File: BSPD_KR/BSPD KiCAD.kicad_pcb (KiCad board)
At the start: 2 copper layers, 52.2 x 80.9 mm, 71 parts, among them J1 Conn_01x03, J2 Conn_01x02, J3 Conn_01x02, K1 G5Q-1A4-DC12, Q1 2N7002, Q3 2N7002, U18 SN74AHCT1G08DBVR, U19 LM339N, U4 LM7805MPX/NOPB, U5 LM339N, U6 SN74AHC1G02DBVR, U9 SN74LVC1G04DBVT

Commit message: feat(bspd): lay out SR latch on PCB, fix board outline and via drill
Place U20/U21 (SN74AHC1G02 latch) on the bottom side under R30/D10,
R30/D10/C13 on the freed R19/R21/C11 sites and C14 decoupling below.
Route the new nets with Freerouting; existing nets unchanged within
1.5 mm. Drop C15 (one shared decoupling cap is enough for two adjacent
gates) and switch D10 to the DO-41 footprint already used by D9.

Also close the Edge.Cuts outline (small endpoint mismatches made the
Specctra exporter reject the board) and raise via drill to 0.3 mm to
meet the board's own min-hole constraint. DRC: 0 errors, 0 unconnected.

Co-Authored-By: Claude Fable 5.1 <noreply@anthropic.com>
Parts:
- removed C11: 10uF, Capacitor_THT:CP_Radial_D5.0mm_P2.50mm
- removed Q3: 2N7002, Package_TO_SOT_SMD:SOT-23
- removed R19: 1k, Resistor_THT:R_Axial_DIN0207_L6.3mm_D2.5mm_P10.16mm_Horizontal
- removed R21: 1M, Resistor_THT:R_Axial_DIN0207_L6.3mm_D2.5mm_P10.16mm_Horizontal
- added C13: 0.22uF, Kicad_Libraries:FA14X7R1H224KNU00, F.Cu at (-176.6, 108.7)
- added C14: 0.1uF, Kicad_Libraries:FA18X7R1H104KNU00, F.Cu at (-168.5, 109.8)
- added D10: 1N4148, Diode_THT:D_DO-41_SOD81_P10.16mm_Horizontal, F.Cu at (-171.0, 106.7)
- added R30: 470k, Resistor_THT:R_Axial_DIN0207_L6.3mm_D2.5mm_P10.16mm_Horizontal, F.Cu at (-160.9, 103.3)
- added U20: SN74AHC1G02DBVR, Package_TO_SOT_SMD:SOT-23-5, B.Cu at (-165.5, 103.3)
- added U21: SN74AHC1G02DBVR, Package_TO_SOT_SMD:SOT-23-5, B.Cu at (-165.5, 107.0)
- R20: value 56k -> 39k
- renumbered REF** to H1, REF** to H2, REF** to H3, REF** to H4
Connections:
- U5 pad 8: /10s -> /LATCH_Q
- U9 pad 4: Net-(Q3-G) -> /BSPD_TRIP
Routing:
- net /POR: track 0.00 -> 18.9 mm
- net /10s: track 17.3 -> 0.00 mm
- net /LATCH_Q: track 0.00 -> 14.8 mm
- net /BSPD_TRIP: track 0.00 -> 13.7 mm, vias 0 -> 1
- net /LATCH_QN: track 0.00 -> 8.36 mm
- net +5V: track 231.5 -> 238.1 mm
- net Net-(Q3-G): track 5.63 -> 0.00 mm
- net Net-(Q3-S): track 2.62 -> 0.00 mm
- net GLV-: track 0.00 -> 2.00 mm, vias 0 -> 2
- net Net-(R26-Pad1): track 45.2 -> 46.5 mm
- net Net-(R13-Pad1): track 35.3 -> 36.6 mm
- net Net-(U5A--): track 21.1 -> 22.0 mm
- net Net-(R15-Pad1): track 44.3 -> 45.0 mm
- net GLV+: track 76.7 -> 77.3 mm

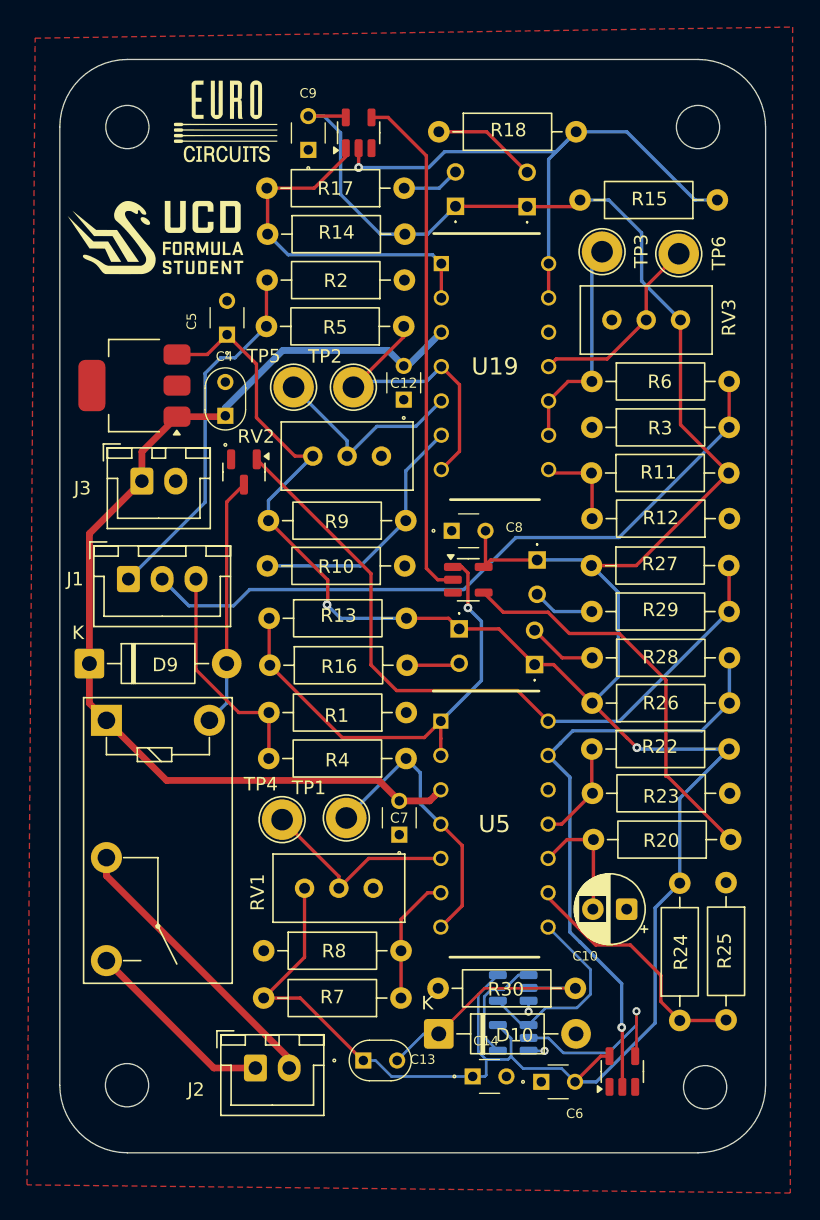
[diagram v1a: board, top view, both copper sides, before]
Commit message: fix(bspd): correct C10 electrolytic polarity, harden POR, enforce 0.25mm tracks
Full-chain behavioural sim (analysis/helpers/bspd_system.cir) showed the
POR pulse (220n/470k) could fall short of the AHC input threshold on a
slow 5V ramp, leaving the latch powered up in the tripped state. C13 is
now 10uF/100k (tau 1s), passing the worst-case ramp with margin.

The same pass found C10 (500ms timer cap) fitted with its positive pad on
GND while the timer node swings 0-5V; swapped the symbol orientation and
pad nets so the cap is forward biased. C13 uses the same part and
footprint. J2 nudged 0.5mm to clear the larger cap.

Re-routed the new nets with Freerouting at the board's 0.25mm minimum
track width (netclass default was 0.2, below the constraint). DRC: 0
errors, 0 unconnected; all pad nets match the schematic netlist.

Co-Authored-By: Claude Fable 5.1 <noreply@anthropic.com>
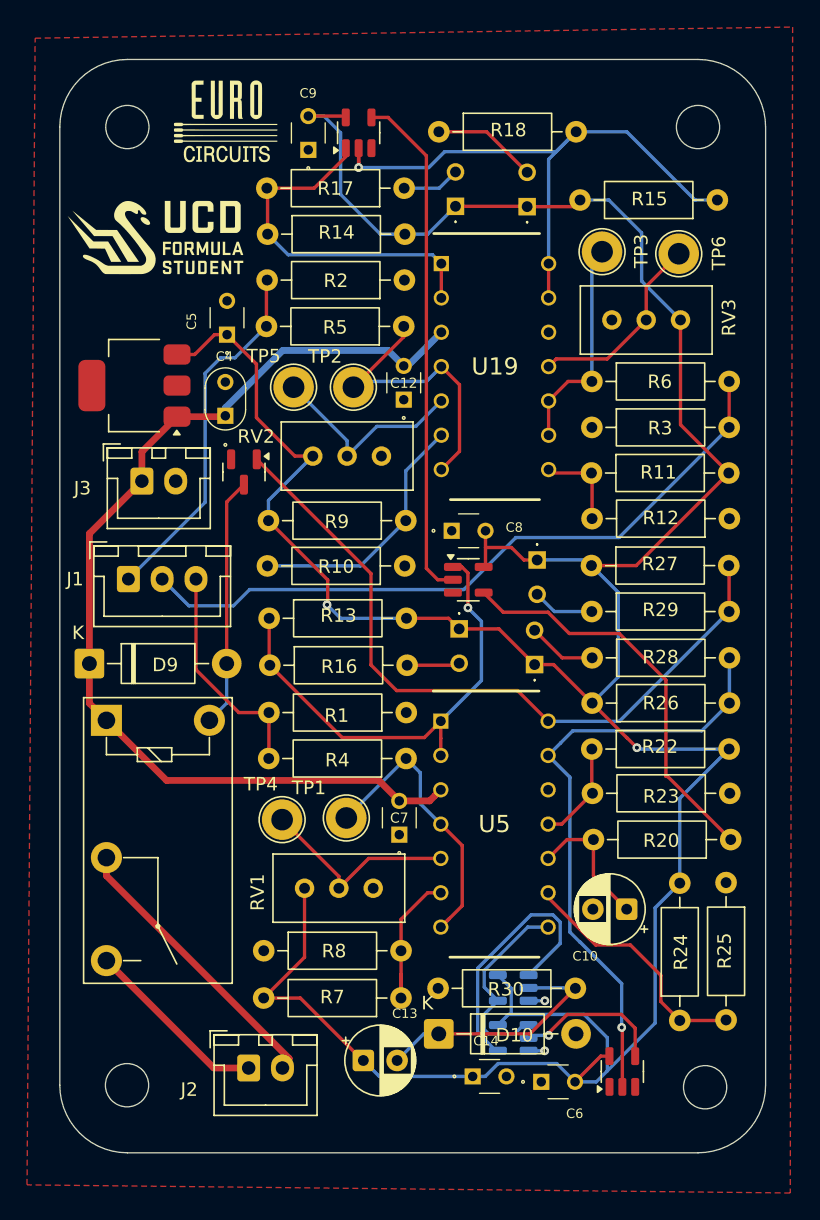
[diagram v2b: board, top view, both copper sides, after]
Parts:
- C13: value 0.22uF -> 10uF; footprint Kicad_Libraries:FA14X7R1H224KNU00 -> Capacitor_THT:CP_Radial_D5.0mm_P2.50mm
- moved J2 0.50 mm to (-185.1, 109.2)
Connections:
- C10 pad 1: GLV- -> /500ms
- C10 pad 2: /500ms -> GLV-
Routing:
- net /LATCH_QN: track 8.36 -> 19.7 mm
- net +5V: track 238.1 -> 242.0 mm
- net /BSPD_TRIP: track 13.7 -> 11.2 mm
- net Net-(U5B--): track 9.58 -> 11.3 mm
- net Net-(R26-Pad1): track 46.5 -> 45.2 mm
- net Net-(R13-Pad1): track 36.6 -> 35.3 mm
- net /500ms: track 9.10 -> 10.1 mm
- net BSPD_Shutdown+: track 14.3 -> 13.8 mm

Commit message: fix(bspd): sync PCB fields with schematic, refresh BOMs, add fab outputs
PCB footprint fields lagged the schematic after the latch/POR changes:
R30 still read 470k (schematic 100k), R20's part number was 56K (now
39K), D10 carried stale 1N4001 MPN/LCSC/datasheet fields, and Q1 had no
part number. Synced every field from the schematic via pcbnew; copper
and placement are untouched. DRC schematic parity now reports only the
H1-H4 mounting holes, which are PCB-only by design.

The root BOMs (BSPD BOM.csv, BSPD BOM_smd.csv) still listed the old RC
timer parts (Q3, R19, R21 1M, C11) and none of the latch ICs.
Regenerated them from the schematic in the same column format.

Adds fab/ (gerbers, drill, BOM, CPL) for the prototype order. The CPL
is regenerated for R30's value; the gerbers are unaffected because no
Fab layer is plotted. Also adds analysis/helpers/bspd_system.cir, the
full-chain sim cited in 69582c7.

Co-Authored-By: Claude Opus 5.5 <noreply@anthropic.com>
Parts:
- R30: value 470k -> 100k
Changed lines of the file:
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@@
 			)
 		)
-		(property "Part Number" "MCF 0.25W 56K"
+		(property "Part Number" "MCF 0.25W 39K"
 			(at 0 0 180)
 			(unlocked yes)
@@
 			)
 		)
-		(property "Datasheet" "http://www.vishay.com/docs/88503/1n4001.pdf"
+		(property "Datasheet" ""
 			(at 0 0 0)
 			(layer "F.Fab")
@@
 			)
 		)
-		(property "Description" ""
+		(property "Description" "Diode, small symbol"
 			(at 0 0 0)
 			(layer "F.Fab")
@@
 			)
 		)
-		(property "Manufacturer" "(MDD) Jiangsu Yutai Elec"
+		(property "Manufacturer" ""
 			(at 0 0 0)
 			(unlocked yes)
@@
 			)
 		)
-		(property "Manufacturer Part Number" "1N4001"
+		(property "Manufacturer Part Number" ""
 			(at 0 0 0)
 			(unlocked yes)
@@
 			)
 		)
-		(property "Store" "LCSC"
+		(property "Store" ""
 			(at 0 0 0)
 			(unlocked yes)
@@
 			)
 		)
-		(property "Store Part Number" "C2456"
+		(property "Store Part Number" ""
 			(at 0 0 0)
 			(unlocked yes)
@@
 			)
 		)
-		(property "Description" ""
+		(property "Description" "Unpolarized capacitor, small symbol"
 			(at 0 0 0)
 			(layer "F.Fab")
@@
 			)
 		)
+		(property "Part Number" "2N7002"
+			(at 0 0 0)
+			(layer "F.Fab")
+			(hide yes)
+			(effects
+				(font
+					(size 1.27 1.27)
+				)
+			)
+		)
 		(property ki_fp_filters "SOT?23*")
 		(sheetname "/")
@@
 			)
 		)
-		(property "Value" "470k"
+		(property "Value" "100k"
 			(at 5.08 2.37 0)
 			(layer "F.Fab")
@@
 			)
 		)
-		(property "Datasheet" "https://www.farnell.com/datasheets/3436052.pdf?_gl=1*6igt67*_gcl_au*OTY1ODIxNDc3LjE3MzU0MDg2OTk."
+		(property "Datasheet" ""
 			(at 0 0 0)
 			(layer "F.Fab")
@@
 			)
 		)
-		(property "Description" ""
+		(property "Description" "Resistor, small symbol"
 			(at 0 0 0)
 			(layer "F.Fab")
@@
 			)
 		)
-		(property "Part Number" "MCF 0.25W 470K"
+		(property "Part Number" "MCF 0.25W 100K"
 			(at 0 0 180)
 			(unlocked yes)
@@
 			)
 		)
-		(property "Description" ""
+		(property "Description" "Unpolarized capacitor, small symbol"
 			(at 0 0 0)
 			(layer "F.Fab")
@@
 			)
 		)
-		(property "Datasheet" "https://www.ti.com/lit/ds/symlink/sn74ahc1g02.pdf?ts=1738520903275"
+		(property "Datasheet" "https://www.ti.com/lit/ds/symlink/sn74ahc1g02.pdf"
 			(at 0 0 0)
 			(layer "B.Fab")
@@
 			)
 		)
-		(property "Datasheet" "https://www.ti.com/lit/ds/symlink/sn74ahc1g02.pdf?ts=1738520903275"
+		(property "Datasheet" "https://www.ti.com/lit/ds/symlink/sn74ahc1g02.pdf"
 			(at 0 0 0)
 			(layer "B.Fab")

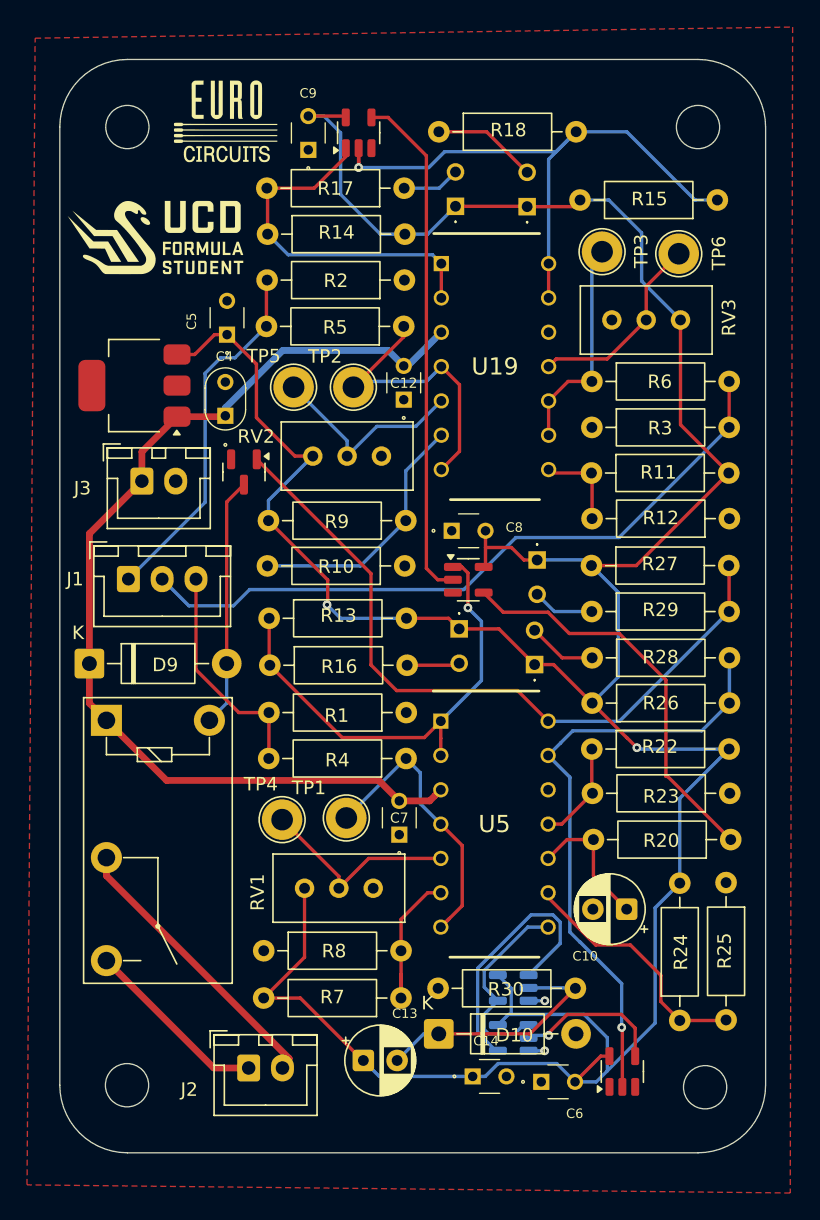
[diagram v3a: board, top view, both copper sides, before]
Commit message: feat(bspd): trip on any single sensor fault, lower missing threshold
An unplugged, open or shorted sensor did not trip the BSPD on its own:
the "sensor missing" comparators were wired-OR into the same wires as
"pressure/current too high", so a dead brake sensor looked like hard
braking and the board waited for high current (and vice versa).
T11.9.2 requires open circuit, short to ground and short to supply on
any SCS to reach the safe state (open SDC).

U5B, U19B and U19D now drive a separate FAULT_N net instead of the
per-sensor wires. Two LM393s (SOIC-8, bottom side, inside the U5/U19
footprints) add over-range checks at 4.74 V for all three sensors on
the same net. R32/C15 debounce FAULT_N (~0.16 s, glitches up to
~0.12 s ignored) and U22B pulls TRIP_REQ_N low, joining the existing
timer output, so a sensor fault latches exactly like an implausibility.

R8/R10/R12 go from 10k to 5.1k, moving the missing threshold from
0.45 V to 0.24 V: the TE M7139 brake sensors sit at 0.5 V at rest,
leaving only 0.05 V of margin before.

PCB: 10 new bottom-side parts. The three moved outputs were branch
points of their sensor wires, so those three spots were rerouted by
hand. New nets were routed with Freerouting with all existing tracks
locked; existing copper is otherwise unchanged. DRC 0 errors and 0
unconnected; parity shows only the H1-H4 mounting holes; the warning
set matches the previous board.

Sim: shared model in bspd_core.inc; bspd_fault_tests.cir covers each
sensor unplugged or shorted to 5 V (all trip in 0.16 s), 50/120 ms
glitches, full-scale and 30 bar braking alone, and late sensor
power-up (none trip). The original timeline results are unchanged.

Regenerated BOMs, fab outputs and the STEP model, which had dated
from before the latch rework. README updated, including the open item
that the current sensor must stay below 4.74 V (~224 A at 10 mV/A).

Co-Authored-By: Claude Opus 5.5 <noreply@anthropic.com>
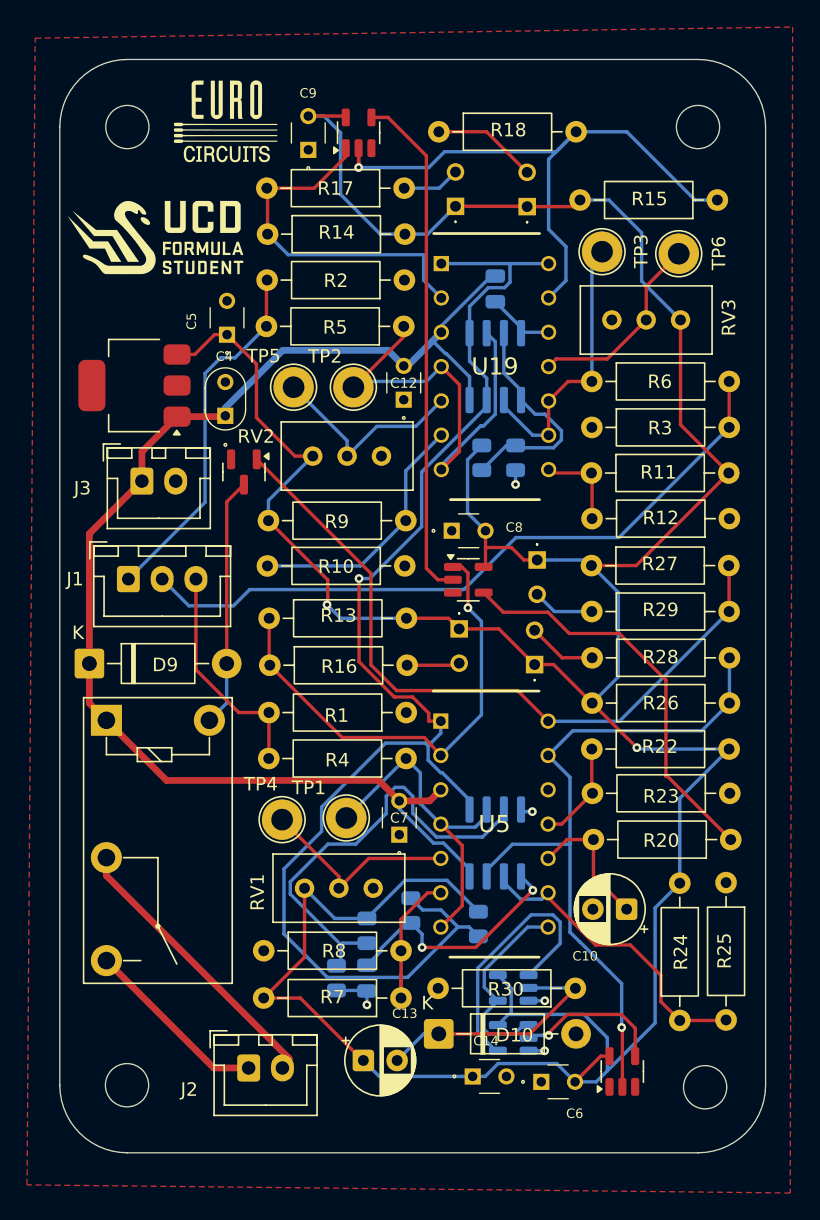
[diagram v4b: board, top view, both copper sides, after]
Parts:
- added C15: 1uF, Capacitor_SMD:C_0805_2012Metric, B.Cu at (-176.3, 102.6)
- added C16: 0.1uF, Capacitor_SMD:C_0805_2012Metric, B.Cu at (-166.8, 51.6)
- added R31: 10k, Resistor_SMD:R_0805_2012Metric, B.Cu at (-168.1, 98.6)
- added R32: 100k, Resistor_SMD:R_0805_2012Metric, B.Cu at (-173.1, 97.6)
- added R33: 1k, Resistor_SMD:R_0805_2012Metric, B.Cu at (-176.3, 99.1)
- added R34: 18k, Resistor_SMD:R_0805_2012Metric, B.Cu at (-178.6, 102.6)
- added R35: 1k, Resistor_SMD:R_0805_2012Metric, B.Cu at (-167.8, 64.1)
- added R36: 18k, Resistor_SMD:R_0805_2012Metric, B.Cu at (-165.3, 64.1)
- added U22: LM393, Package_SO:SOIC-8_3.9x4.9mm_P1.27mm, B.Cu at (-166.8, 92.6)
- added U23: LM393, Package_SO:SOIC-8_3.9x4.9mm_P1.27mm, B.Cu at (-166.8, 57.3)
- R10, R12, R8: value 10k -> 5.1k
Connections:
- net Net-(R26-Pad1) renamed /TRIP_REQ_N
- net Net-(U19A--) renamed /SENS_FRONT
- net Net-(U19C--) renamed /SENS_REAR
- net Net-(U5A--) renamed /SENS_CUR
- net Net-(U5D-+) renamed /REF_1V0
- U19 pad 1: Net-(R14-Pad1) -> /FAULT_N
- U19 pad 14: Net-(R15-Pad1) -> /FAULT_N
- U5 pad 1: Net-(R13-Pad1) -> /FAULT_N
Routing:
- net /FAULT_N: track 0.00 -> 103.1 mm, vias 0 -> 1
- net /OVR_REF_CUR: track 0.00 -> 32.7 mm
- net +5V: track 242.0 -> 265.3 mm
- net GLV+: track 77.3 -> 97.0 mm
- net /FAULT_F: track 0.00 -> 18.2 mm, vias 0 -> 2
- net /OVR_REF_BRK: track 0.00 -> 17.0 mm
- net /SENS_FRONT: track 22.1 -> 34.2 mm
- net GLV-: track 2.39 -> 12.8 mm, vias 2 -> 5
- net /TRIP_REQ_N: track 45.2 -> 52.6 mm
- net /SENS_REAR: track 16.2 -> 20.9 mm
- net /REF_1V0: track 18.5 -> 22.9 mm
- net /SENS_CUR: track 22.0 -> 26.3 mm
- net Net-(R15-Pad1): track 44.7 -> 45.7 mm
